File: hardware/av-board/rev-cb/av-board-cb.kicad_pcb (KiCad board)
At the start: 4 copper layers, 100 x 100 mm, 294 parts, among them J1 RCA Y, J11 XIAO 5V..D7, J12 XIAO D0..D6, J13 SPDIF, J15 USB-C 5V, J16 JTAG, J2 RCA Pb, J20 DF40HC(3.0)-80DS, J21 DF40HC(3.0)-100DS, J22 DF40HC(3.0)-100DS, J3 RCA Pr, J4 RCA L, J5 RCA R, J6 HDMI-001, J7 SYNC, J8 VGA, Q1 2N7002, Q2 2N7002, Q3 2N7002, Q4 2N7002, Q5 2N7002, SW1 TS-1187A-B-A-B, SW2 TS-1187A-B-A-B, SW3 TS-1187A-B-A-B, U1 ADV7181DBCPZ-RL, U10 TPD4E05U06DQAR, U12 TPS7A2045PDBVR, U13 SN74LVC1GU04DBVR, U14 SN74LVC1G04DBVR, U15 SN74LVC1G04DBVR, U17 MS5351M, U18 ME6211C25M5G-N, U19 TPD4E05U06DQAR, U2 SN65DP159RGZR, U20 TPD4E05U06DQAR, U21 SN74LVC2G17DBVR, U22 SN74LVC8T245PWR, U23 SN74AVC4T245PWR, U24 ME6211C30M5G-N, U3 PCM1808PWR, U4 TLV62569DBVR, U5 TPS7A7001DDAR, U6 TPS7A7001DDAR, U7 TLV62569DBVR, U8 TPD4E05U06DQAR, U9 TPD4E05U06DQAR, Y1 28.63636MHz 20pF, Y2 25MHz 10pF

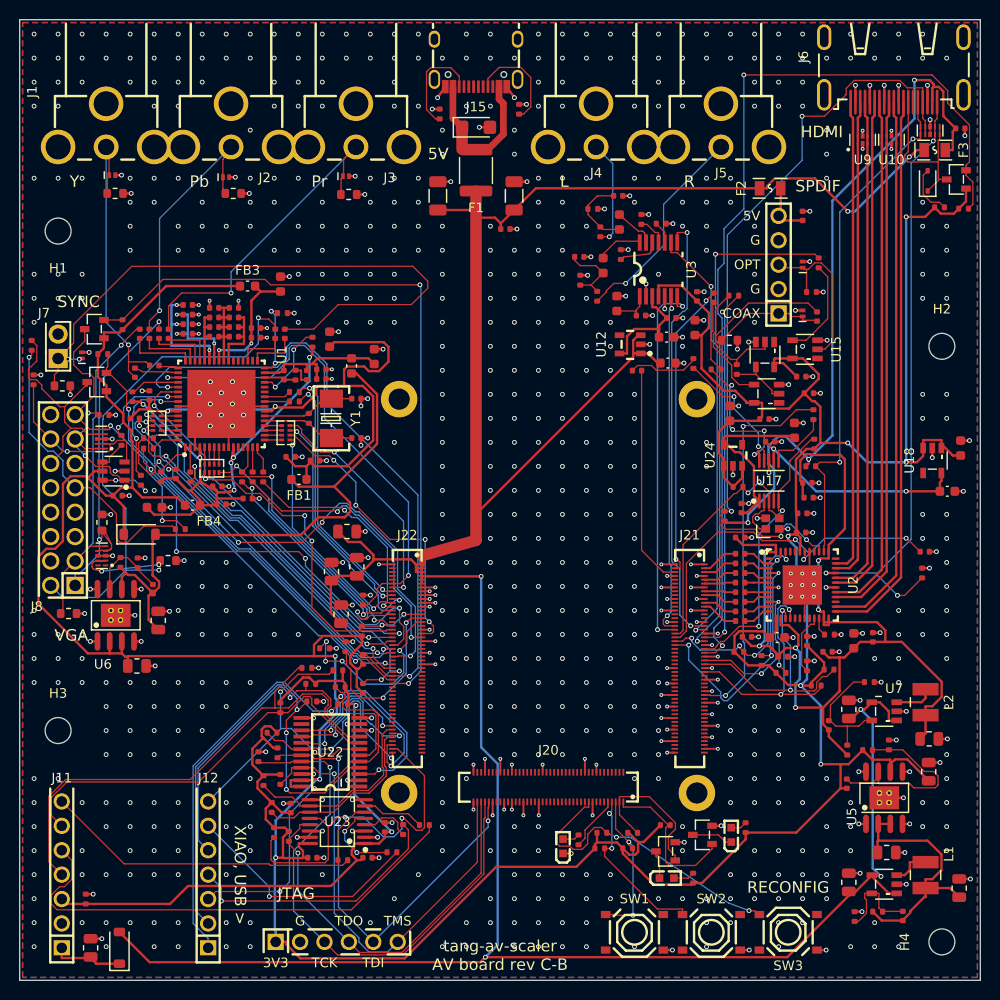
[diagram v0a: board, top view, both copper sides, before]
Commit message: AV board C-B: a protected debug header and test pads; the kit on KiCad 10, a second host
C-B (the SOM hides the FPGA's pins, so the board brings out what bring-up needs):
- J17, a 2 x 8 header left of the SOM: the ADV7181D's, the DP159's and the MS5351M's I2C, six
  spare FPGA pins, J22's nearest (dbg0-dbg5: AB16 L13 M13 AA16 AB17 Y17, LVCMOS33 in
  fpga/av-board-cb.cst), a 3.3 V reference and ground, labelled pin by pin, "DEBUG" above it.
  Every pin but ground through 220 R by the header (C25091, as Digilent's Pmod ports): a slipped
  probe or a wrong wire drives at most 15 mA into a pin; VREF, beside ground, is a reference
  (50 mW in its resistor when shorted), not a supply.
- A bare test pad on each rail by its regulator (+5V 3V6 3V3 1V8 1V1 3V0 2V5 5VA), labelled,
  and two ground pads with holes for a wire loop. Not assembled.
- The DP159's ground pins 19 and 41 now reach into its exposed pad: their fanout stubs stopped
  0.22 mm short of it, the prune pass took them up, and pin 19 was left open
  (gen_pcb.py serdes()).
- Re-routed: the best of a batch (v5): DRC 0 errors, 0 unconnected; schematic = board.py =
  board (1064 pins); fab files, renders and rev-c/review.md's layout numbers updated. Three
  resistors after the debug block are renumbered (R100-R102 -> R113-R115).
- Known, fixes next: an HDMI 2.0 layout audit against TI's SN65DP159 and SPRAAR7 guidelines
  finds other nets' vias against the TMDS run (their plane antipads within 0.01-0.21 mm),
  pairs 3W apart (TI: 5W), the transceivers' reference clock autorouted as two single lines,
  a crystal and a mounting hole near the lines, and no plane voids under the pads on them.

rev-c/review.md: kit/xtalk.py measures analog tracks against digital tracks only; KiCad's DRC
with the 0.5 mm rule as a custom rule counts vias too, and finds two of RCA_SYNC's vias 0.27 mm
from the VGA DDC clock on C-A (the C-A text said nothing but XTAL1/LLC came that close).

Kit:
- main(): the board made with its project (pcbn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
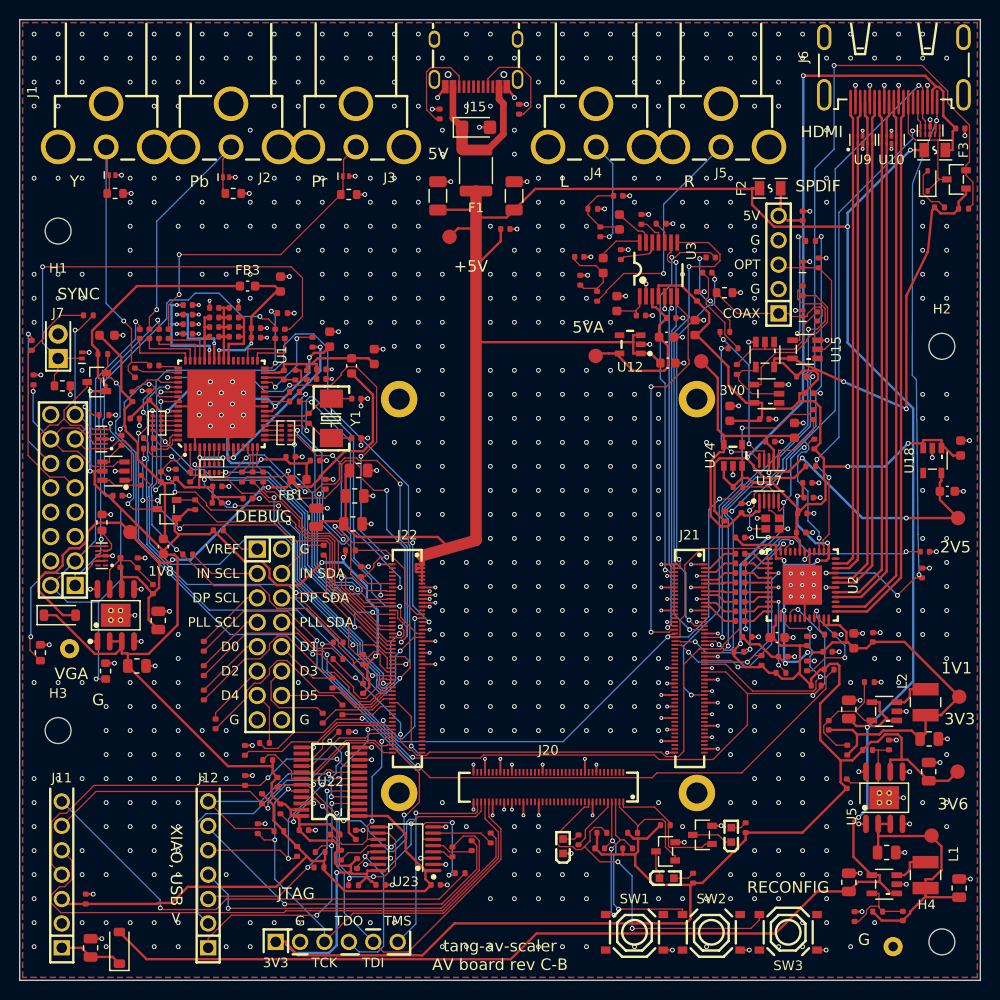
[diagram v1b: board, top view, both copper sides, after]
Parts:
- added J17: DEBUG, lcsc:HDR-TH_16P-P2.54-V-M-R2-C8-S2.54, F.Cu at (126.0, 114.0)
- added R103: 220, Resistor_SMD:R_0402_1005Metric, F.Cu at (119.2, 115.2)
- added R104: 220, Resistor_SMD:R_0402_1005Metric, F.Cu at (133.2, 114.8)
- added R105: 220, Resistor_SMD:R_0402_1005Metric, F.Cu at (119.2, 117.8)
- added R106: 220, Resistor_SMD:R_0402_1005Metric, F.Cu at (133.1, 116.6)
- added R107: 220, Resistor_SMD:R_0402_1005Metric, F.Cu at (119.2, 120.3)
- added R108: 220, Resistor_SMD:R_0402_1005Metric, F.Cu at (132.6, 119.0)
- added R109: 220, Resistor_SMD:R_0402_1005Metric, F.Cu at (120.4, 123.3)
- added R110: 220, Resistor_SMD:R_0402_1005Metric, F.Cu at (131.5, 122.7)
- added R111: 220, Resistor_SMD:R_0402_1005Metric, F.Cu at (125.5, 125.3)
- added R112: 220, Resistor_SMD:R_0402_1005Metric, F.Cu at (133.6, 121.8)
- added R113: 1k, Resistor_SMD:R_0402_1005Metric, F.Cu at (134.4, 105.2)
- added R114: 5.1k, Resistor_SMD:R_0402_1005Metric, F.Cu at (123.4, 126.1)
- added R115: 5.1k, Resistor_SMD:R_0402_1005Metric, F.Cu at (131.9, 98.4)
- added TP1: +5V, TestPoint:TestPoint_Pad_D1.5mm, F.Cu at (144.8, 72.6)
- added TP10: GND, TestPoint:TestPoint_THTPad_D2.0mm_Drill1.0mm, F.Cu at (105.2, 115.5)
- added TP2: 3V6, TestPoint:TestPoint_Pad_D1.5mm, F.Cu at (194.9, 134.9)
- added TP3: 3V3, TestPoint:TestPoint_Pad_D1.5mm, F.Cu at (197.6, 128.3)
- added TP4: 1V8A, TestPoint:TestPoint_Pad_D1.5mm, F.Cu at (111.5, 103.3)
- added TP5: 1V1, TestPoint:TestPoint_Pad_D1.5mm, F.Cu at (197.8, 120.5)
- added TP6: 3V0, TestPoint:TestPoint_Pad_D1.5mm, F.Cu at (171.0, 85.6)
- added TP7: 2V5, TestPoint:TestPoint_Pad_D1.5mm, F.Cu at (197.7, 101.9)
- added TP8: 5VA, TestPoint:TestPoint_Pad_D1.5mm, F.Cu at (160.0, 85.0)
- added TP9: GND, TestPoint:TestPoint_THTPad_D2.0mm_Drill1.0mm, F.Cu at (190.9, 146.5)
- R100: value 1k -> 220
- R101, R102: value 5.1k -> 220
- moved R40 24.2 mm to (107.1, 80.8)
- moved Q2 20.2 mm to (115.3, 100.9)
- moved R39 20.2 mm to (118.3, 100.5)
- moved R101 19.0 mm to (117.5, 105.7), turned to 0 degrees
- moved R60 18.9 mm to (131.2, 138.2)
- moved C16 18.6 mm to (109.1, 82.8)
- moved R100 18.3 mm to (120.7, 103.2), turned to 0 degrees
- moved R62 17.8 mm to (127.0, 134.5)
- moved R61 17.5 mm to (128.9, 136.6), turned to 90 degrees
- moved R58 15.6 mm to (131.3, 136.7)
- moved R72 14.4 mm to (134.8, 140.1), turned to 0 degrees
- moved C83 14.1 mm to (171.9, 74.8)
- moved R64 13.4 mm to (123.5, 129.2), turned to 90 degrees
- moved R31 13.2 mm to (108.9, 117.8), turned to 90 degrees
- moved C109 12.4 mm to (134.9, 99.6), turned to 0 degrees
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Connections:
- J22 pad 26: (no net) -> DBG5
- J22 pad 28: (no net) -> DBG4
- J22 pad 30: (no net) -> DBG3
- J22 pad 32: (no net) -> DBG2
- J22 pad 34: (no net) -> DBG1
- J22 pad 36: (no net) -> DBG0
- R100 pad 2: MODE0 -> DBG_VREF
- R101 pad 1: MODE1 -> IN_SCL
- R101 pad 2: GND -> IN_SCL_J
- R102 pad 1: MODE2 -> IN_SDA
- R102 pad 2: GND -> IN_SDA_J
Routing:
- net DP_SCL: track 25.6 -> 105.4 mm, vias 2 -> 4
- net PLL_SCL: track 24.0 -> 86.4 mm, vias 2 -> 3
- net DP_SDA: track 25.4 -> 82.9 mm, vias 2 -> 4
- net PLL_SDA: track 29.3 -> 84.6 mm, vias 2 -> 5
- net VGA_SCL_F: track 78.6 -> 34.4 mm
- net DBG4: track 0.00 -> 29.2 mm, vias 0 -> 2
- net XIAO_D0: track 57.9 -> 30.4 mm
- net DBG0: track 0.00 -> 26.4 mm
- net 3V3: track 464.0 -> 489.1 mm, vias 9 -> 12
- net DBG2: track 0.00 -> 24.7 mm
- net IN_Y6: track 40.7 -> 64.8 mm
- net 1V1: track 108.9 -> 86.8 mm, vias 6 -> 7
- net IN_C7: track 22.5 -> 43.1 mm, vias 2 -> 4
- net ESP_IRQ: track 37.6 -> 19.0 mm
- net XIAO_D4: track 40.7 -> 22.7 mm, vias 1 -> 2
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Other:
- board text added: "+5V"
- board text added: "1V1"
- board text added: "1V8"
- board text added: "2V5"
- board text added: "3V0"
- board text added: "3V6"
- board text added: "5VA"
- board text added: "D0"
- board text added: "D1"
- board text added: "D2"
- board text added: "D3"
- board text added: "D4"
- board text added: "D5"
- board text added: "DEBUG"
- board text added: "DP SCL"
- board text added: "DP SDA"
- board text added: "IN SCL"
- board text added: "IN SDA"
- board text added: "PLL SCL"
- board text added: "PLL SDA"
- board text added: "VREF"

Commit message: AV board C-B: the HDMI lines to TI's layout rules; the reference clock laid as a pair
C-B, after an audit against the published HDMI layout rules (TI's SN65DP159 data sheet,
SPRAAR7 and HDMI Design Guide, Intel AN 837; the specification itself is for Adopters only):
rev-c/review.md's new HDMI rows, kit/hdmi_audit.py.
- The TMDS pairs 1.27 mm apart along their run (5 W at 0.25 mm lines, SPRAAR7 3.1), closing to
  the ESD arrays' 0.75 mm within the receptacle's break-out; they were 0.75 mm (3 W) all the way.
- Rule areas beside and between the pairs on F.Cu keep out other tracks, vias and the ground
  pour: 3V3, 2V5, +5V and DP_OE vias had stood beside the outer lines, their In1 antipads
  0.01-0.21 mm from them (1.5 W asked). In1 and In2 voided under the lanes' AC capacitors' pads
  and 60 % of the ESD arrays' TMDS pads (SPRAAR7 3.10, 3.14).
- The transceivers' reference clock laid by the generator as a pair: 0.2 mm lines 0.2 mm apart,
  24.4 and 26.5 mm from the MS5351M's pins, no vias, its 2.2 R and 100 nF side by side at the
  pins. It was two autorouted lines, 33-39 mm with two vias each, 0.15 mm from the PCM1808's
  bit clock: the placer had put its parts 20-30 mm off. A REFCLK net class: the router keeps
  other lines 30 mil off and clocks 50 mil (the PCM1808's clocks now in CLOCK).
- The MS5351M 0.5 mm right, for the pair's parts; its crystal held up against it, 3.1 mm off the
  lines (was 1.6 mm from DP_D2_P).
- J21's ground pins 94 and 100 take their vias inward, out of the pair's way; two inward vias
  facing each other across a receptacle share one (rev-c/layout.py som_fanout: their drills
  stood 0.08 mm apart). C-A has no inward vias: unchanged.
- Re-routed (the best of a batch, z4): DRC 0 errors, 0 unconnected; schematic = board.py =
  board (1064 pins); the generator's placement and copper reproduced on the routed board (to
  the router's 0.1 um rounding). Fab files, renders and the review's numbers updated.
- Open: H2's hole edge 2.1 mm from the TMDS 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
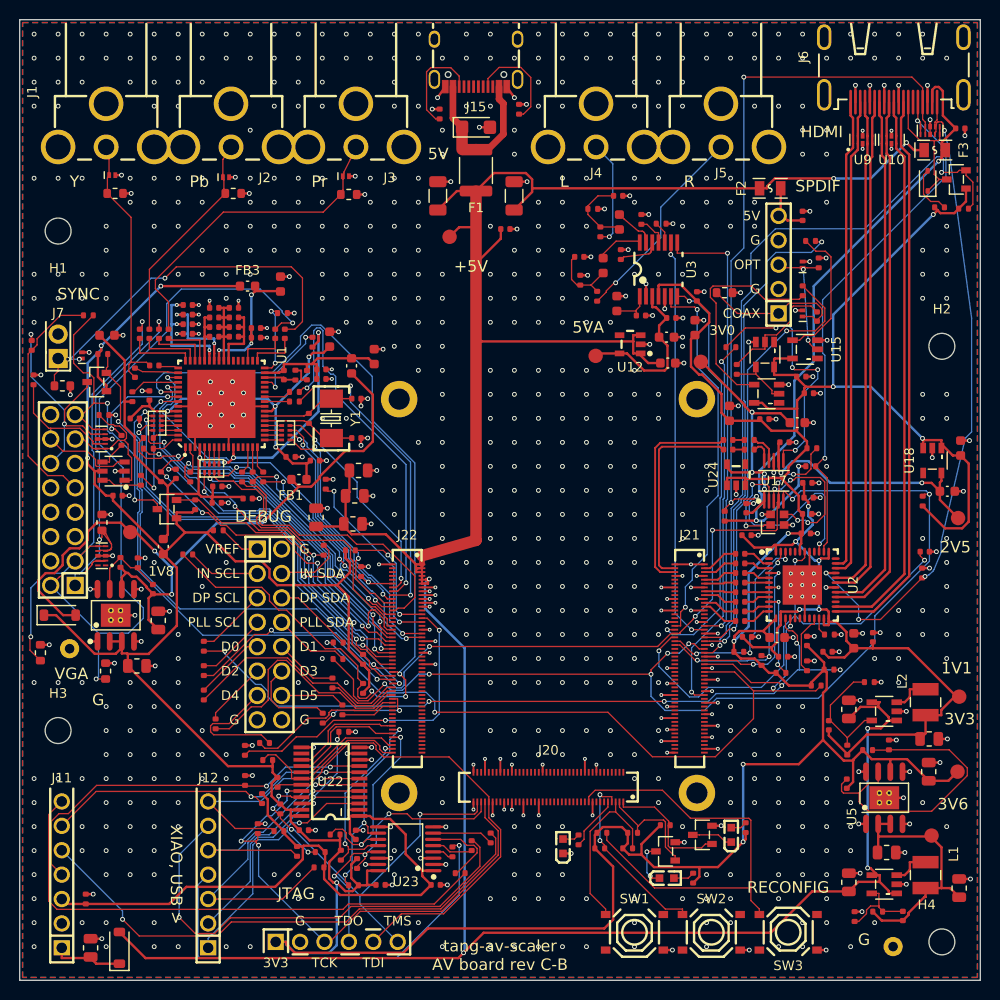
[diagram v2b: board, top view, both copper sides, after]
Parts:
- moved C83 19.1 mm to (173.8, 93.8), turned to 180 degrees
- moved C82 18.5 mm to (173.8, 94.8), turned to 180 degrees
- moved R86 12.7 mm to (194.0, 100.1)
- moved R89 11.5 mm to (175.9, 93.8), turned to 180 degrees
- moved R87 11.1 mm to (174.0, 84.1), turned to 0 degrees
- moved R88 10.7 mm to (175.9, 94.8), turned to 180 degrees
- moved R85 8.68 mm to (182.5, 94.6)
- moved U24 2.05 mm to (174.6, 97.4)
- moved C81 1.49 mm to (179.6, 94.0)
- moved C77 0.86 mm to (181.0, 91.9), turned to 0 degrees
- moved C105 0.71 mm to (175.7, 103.7)
- moved Y2 0.64 mm to (178.9, 102.0)
- moved C99 0.50 mm to (182.0, 101.5)
- moved C98 0.50 mm to (181.8, 103.5)
- moved C80 0.50 mm to (175.6, 100.8)
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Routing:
- net IN_SCL: track 52.5 -> 100.4 mm, vias 2 -> 4
- net PLL_SDA: track 84.6 -> 109.7 mm, vias 5 -> 7
- net FB_3V3: track 8.56 -> 32.6 mm
- net IN_Y6: track 64.8 -> 43.8 mm
- net PLL_CLK2_S: track 6.68 -> 26.3 mm, vias 0 -> 4
- net IN_SDA: track 66.1 -> 47.2 mm, vias 3 -> 4
- net CEC_FPGA: track 95.9 -> 77.1 mm
- net DP_SCL: track 105.4 -> 86.6 mm, vias 4 -> 6
- net HDMI_SDA: track 72.7 -> 91.4 mm, vias 3 -> 4
- net +5V: track 329.4 -> 312.1 mm, vias 4 -> 6
- net SER_REFCLK_N: track 39.3 -> 22.1 mm, vias 2 -> 0
- net HDMI_5V: track 84.5 -> 69.1 mm, vias 2 -> 3
- net DP_OE: track 36.8 -> 50.4 mm
- net IN_C7: track 43.1 -> 29.8 mm, vias 4 -> 0
- net IN_C0: track 27.0 -> 40.2 mm
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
